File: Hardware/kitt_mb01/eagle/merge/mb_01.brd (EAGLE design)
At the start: 160 x 100 mm, 126 parts, among them CON1 ARDUINO_UNO, IC1.01 RT8293A, IC2.00 BQ24266RGET, IC3.01 LSM9DS1, J1 CON_HEADER_1X06-SMD-RIGHT-ANG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, J2 CON_HEADER_1X06-SMD-RIGHT-ANG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, P2 S2B-PH-K-S(LF)(SN), U1 MCP23017-E, U6.01 TPS61032RSARPSDO-G16, U7.01 SI1922EDH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

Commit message: snapshot of board merge : fancy pants edition -> added posh silk-screen logo    (possibly too large, still)
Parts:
- removed J1, J2: CON_HEADER_1X06-SMD-RIGHT-ANGLED, dp_devices:M1X6_MALE_RIGHT_ANGLED_SMD
- removed JP3: (no value), pinhead:1X18/90
- removed U1: MCP23017-E, kitt.ic:SOIC28-1.27-17.9X7.5MM
- added REF2: REF.LOGO.UASUA, kitt.refs:REF_LOGO_UASUA
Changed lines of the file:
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@@
 <grid distance="12.5" unitdist="mil" unit="mil" style="lines" multiple="1" display="yes" altdistance="0.0125" altunitdist="inch" altunit="inch"/>
 <layers>
-<layer number="1" name="Top" color="4" fill="1" visible="yes" active="yes"/>
-<layer number="2" name="Route2" color="29" fill="0" visible="yes" active="yes"/>
-<layer number="3" name="Route3" color="24" fill="9" visible="yes" active="yes"/>
+<layer number="1" name="Top" color="4" fill="1" visible="no" active="yes"/>
+<layer number="2" name="Route2" color="29" fill="0" visible="no" active="yes"/>
+<layer number="3" name="Route3" color="24" fill="9" visible="no" active="yes"/>
 <layer number="14" name="Route14" color="1" fill="6" visible="no" active="no"/>
 <layer number="15" name="Route15" color="4" fill="6" visible="no" active="no"/>
@@
 <element name="R0.04" library="rcl" package="R1206" value="[0R]" x="53.6575" y="45.085" rot="MR0"/>
 <element name="JMP2" library="jump-0r-smd" package="A0R-JMP" value="0R-JUMPA" x="50.165" y="50.8" rot="R270"/>
-<element name="U1" library="kitt.ic" package="SOIC28-1.27-17.9X7.5MM" value="MCP23017-E" x="22.38375" y="69.37375">
-<attribute name="MF" value="Microchip" x="22.38375" y="69.37375" size="1.016" layer="27" font="vector" display="off"/>
-<attribute name="AVAILABILITY" value="Good" x="22.38375" y="69.37375" size="1.016" layer="27" font="vector" display="off"/>
-<attribute name="MP" value="MCP23017-E/SO" x="22.38375" y="69.37375" size="1.016" layer="27" font="vector" display="off"/>
-<attribute name="PACKAGE" value="SOIC-28 Microchip" x="22.38375" y="69.37375" size="1.016" layer="27" font="vector" display="off"/>
-<attribute name="DESCRIPTION" value="MCP23017 Series 5.5 V 1.7 MHz SMT 16-Bit I2C I/O Expander - SOIC-28" x="22.38375" y="69.37375" size="1.016" layer="27" font="vector" display="off"/>
-<attribute name="PRICE" value="1.15 USD" x="22.38375" y="69.37375" size="1.016" layer="27" font="vector" display="off"/>
-</element>
 <element name="JP2" library="pinhead" package="2X03/90" value="" x="48.5775" y="39.37" rot="R90"/>
-<element name="JP3" library="pinhead" package="1X18/90" value="" x="4.1275" y="52.07" rot="R90"/>
-<element name="J1" library="dp_devices" package="M1X6_MALE_RIGHT_ANGLED_SMD" value="CON_HEADER_1X06-SMD-RIGHT-ANGLED" x="32.0675" y="52.3875" rot="MR270"/>
-<element name="J2" library="dp_devices" package="M1X6_MALE_RIGHT_ANGLED_SMD" value="CON_HEADER_1X06-SMD-RIGHT-ANGLED" x="25.0825" y="30.48" rot="MR0"/>
 <element name="U$5" library="marks" package="PASS-ROUND" value="" x="67.31" y="46.6725"/>
 <element name="R7,05" library="rcl" package="R0603" value="330R" x="97.155" y="27.94" rot="MR0"/>
@@
 <element name="U$9" library="marks" package="PASSER-CIRCLE" value="" x="102.87" y="71.755"/>
 <element name="REF1" library="kitt.refs" package="REF_LAYERS" value="REF.LAYERS" x="102.5525" y="67.945" rot="R270"/>
+<element name="REF2" library="kitt.refs" package="REF_LOGO_UASUA" value="REF.LOGO.UASUA" x="77.63" y="65.405" rot="MR270"/>
 </elements>
 <signals>

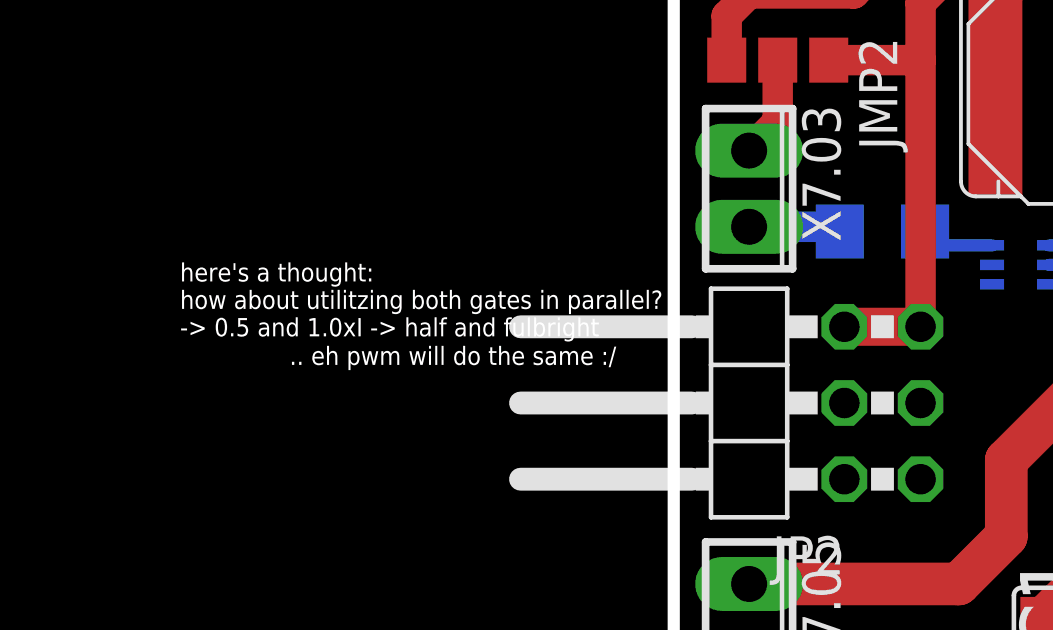
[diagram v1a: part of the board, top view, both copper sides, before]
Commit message: added proper credits in schematics
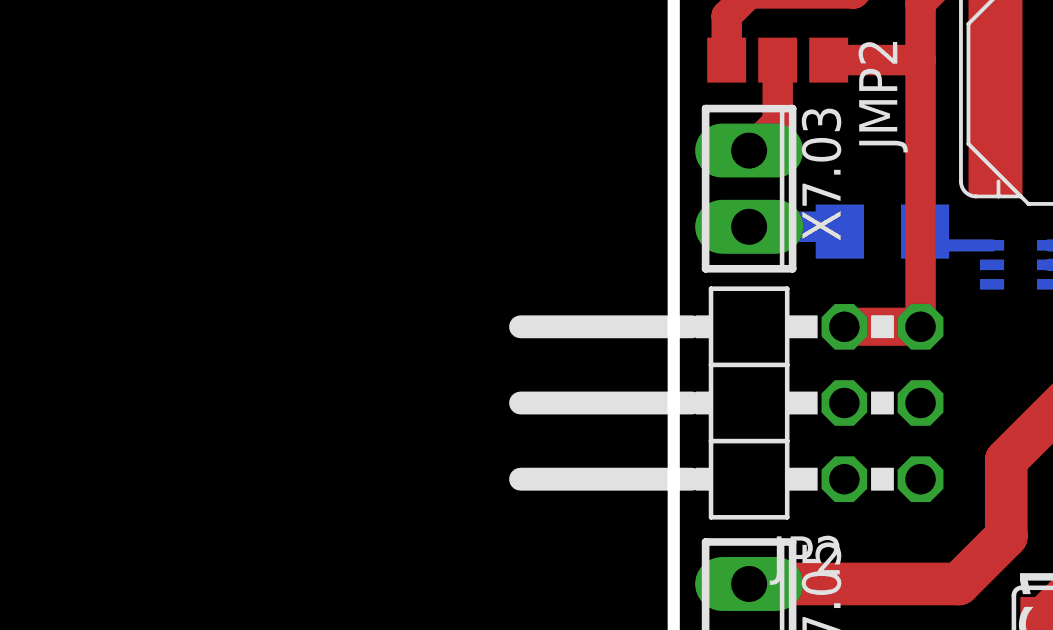
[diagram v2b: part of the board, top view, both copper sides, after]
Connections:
- new net ARDUINO.SCL: IC3.01.2
- new net ARDUINO.SDA: IC3.01.4
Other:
- board text added: "<-- IDK"
- board text added: "ARDUINO<->RAILS"
- board text added: "GROUND POURS"
- board text added: "RAILS POURS"
- board text added: "SPEEDBOARD --> LAPDETECTOR -->"
- board text added: "TODO: COMMAND/BOTTOM LIGHT!!!"
- board text removed: ".. eh pwm will do the same :/"
- board text removed: "here's a thought: how about utilitzing both gates in parallel? -> 0.5 and 1.0xI -> half and fulbright"
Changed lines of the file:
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@@
 <grid distance="12.5" unitdist="mil" unit="mil" style="lines" multiple="1" display="yes" altdistance="0.0125" altunitdist="inch" altunit="inch"/>
 <layers>
-<layer number="1" name="Top" color="4" fill="1" visible="no" active="yes"/>
+<layer number="1" name="Top" color="4" fill="1" visible="yes" active="yes"/>
 <layer number="2" name="Route2" color="29" fill="0" visible="no" active="yes"/>
-<layer number="3" name="Route3" color="24" fill="9" visible="no" active="yes"/>
+<layer number="3" name="Route3" color="24" fill="9" visible="yes" active="yes"/>
 <layer number="14" name="Route14" color="1" fill="6" visible="no" active="no"/>
 <layer number="15" name="Route15" color="4" fill="6" visible="no" active="no"/>
@@
 <text x="45.085" y="47.228125" size="1.778" layer="51" rot="R180">Tail Light --&gt;</text>
 <text x="106.600625" y="46.51375" size="1.778" layer="51">&lt;-- Head Light</text>
-<text x="30.241875" y="41.5925" size="0.6096" layer="46">here's a thought:
-how about utilitzing both gates in parallel?
--&gt; 0.5 and 1.0xI -&gt; half and fulbright</text>
-<text x="33.893125" y="40.64" size="0.6096" layer="46">.. eh pwm will do the same :/</text>
 <hole x="101.6" y="27.94" drill="1.6"/>
+<text x="15.5575" y="52.07" size="1.6764" layer="49" rot="R90">&lt;-- IDK</text>
+<text x="20.32" y="37.7825" size="1.6764" layer="49">SPEEDBOARD --&gt;
+LAPDETECTOR --&gt;</text>
+<text x="70.485" y="11.43" size="1.6764" layer="49">TODO:
+COMMAND/BOTTOM LIGHT!!!</text>
+<text x="70.485" y="8.5725" size="1.778" layer="48">GROUND POURS</text>
+<text x="91.7575" y="8.5725" size="1.778" layer="48">RAILS POURS</text>
+<text x="70.1675" y="6.0325" size="1.778" layer="48">ARDUINO&lt;-&gt;RAILS</text>
 </plain>
 <attributes>
@@
 <wire x1="102.235" y1="59.69" x2="104.775" y2="59.69" width="0" layer="2"/>
 </signal>
+<signal name="ARDUINO.SCL">
+<contactref element="IC3.01" pad="2"/>
+</signal>
+<signal name="ARDUINO.SDA">
+<contactref element="IC3.01" pad="4"/>
+</signal>
 </signals>

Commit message: snapshot of board merge
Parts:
- removed D7.01, D7.02: (no value), led:CHIPLED_1206
- removed R7,03, R7.04: 330R, rcl:R0603
- U$3: value SI1922EDH -> (none); device kitt.ic:SC70-6 -> frames:A4L-LOC
- moved U$3 110.4 mm to (-48.3, -42.5), turned to 0 degrees
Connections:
- removed net N$3: D7.01.C, U$3.6
- removed net N$4: D7.01.A, R7,03.1
- removed net N$5: D7.02.A, R7.04.1
- removed net N$7: D7.02.C, U$3.3
- net +3V3: no longer R7,03.2, R7.04.2
- net GND: no longer U$3.1, U$3.4
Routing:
- net N$7: track 4.12 -> 0.00 mm
- net N$5: track 3.51 -> 0.00 mm
- net GND: track 245.3 -> 242.5 mm
- net N$4: track 1.92 -> 0.00 mm
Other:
- board text added: "D.Hoeginger/A.Gessler"
- board text added: "KITT-MB01 PCB LAYOUT"
- board text added: "Kit for Intelligent and Trainable Trackcars"
- board text removed: "<-- IDK"
- board text removed: "GND@2"
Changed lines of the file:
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@@
 <layers>
 <layer number="1" name="Top" color="4" fill="1" visible="yes" active="yes"/>
-<layer number="2" name="Route2" color="29" fill="0" visible="no" active="yes"/>
+<layer number="2" name="Route2" color="29" fill="0" visible="yes" active="yes"/>
 <layer number="3" name="Route3" color="24" fill="9" visible="yes" active="yes"/>
 <layer number="14" name="Route14" color="1" fill="6" visible="no" active="no"/>
@@
 <wire x1="102.6" y1="73.9" x2="49.1" y2="73.9" width="0.4064" layer="20"/>
 <wire x1="46.7" y1="71.4" x2="46.7" y2="23.1" width="0.4064" layer="20"/>
-<text x="20.16125" y="7.77875" size="1.778" layer="2">GND@2</text>
-<text x="147.32" y="4.60375" size="1.778" layer="2">GND@2</text>
-<text x="143.03375" y="87.78875" size="1.778" layer="2">GND@2</text>
-<text x="8.5725" y="89.8525" size="1.778" layer="2">GND@2</text>
 <text x="48.26" y="64.92875" size="1.9304" layer="25" font="vector">+</text>
 <text x="102.5525" y="35.40125" size="1.016" layer="25" font="vector" rot="R90">SHUNT</text>
@@
 <text x="106.600625" y="46.51375" size="1.778" layer="51">&lt;-- Head Light</text>
 <hole x="101.6" y="27.94" drill="1.6"/>
-<text x="15.5575" y="52.07" size="1.6764" layer="49" rot="R90">&lt;-- IDK</text>
 <text x="20.32" y="37.7825" size="1.6764" layer="49">SPEEDBOARD --&gt;
 LAPDETECTOR --&gt;</text>
@@
 <text x="91.7575" y="8.5725" size="1.778" layer="48">RAILS POURS</text>
 <text x="70.1675" y="6.0325" size="1.778" layer="48">ARDUINO&lt;-&gt;RAILS</text>
+<text x="168.91" y="-22.225" size="1.9304" layer="48" font="vector">D.Hoeginger/A.Gessler</text>
+<text x="114.3" y="-21.9075" size="1.9304" layer="48" font="vector">KITT-MB01 PCB LAYOUT</text>
+<text x="114.3" y="-36.5125" size="1.9304" layer="48" font="vector">Kit for Intelligent and
+Trainable Trackcars</text>
 </plain>
 <attributes>
@@
 <attribute name="MPN" value="" x="102.71125" y="46.51375" size="1.016" layer="27" font="vector" rot="R270" display="off"/>
 </element>
-<element name="D7.01" library="led" package="CHIPLED_1206" value="" x="14.049375" y="43.100625" rot="R270"/>
-<element name="U$3" library="kitt.ic" package="SC70-6" value="SI1922EDH" x="18.176875" y="45.640625" rot="R90"/>
-<element name="R7,03" library="rcl" package="R0603" value="330R" x="14.049375" y="44.688125"/>
-<element name="R7.04" library="rcl" package="R0603" value="330R" x="14.049375" y="46.593125"/>
-<element name="D7.02" library="led" package="CHIPLED_1206" value="" x="14.049375" y="48.180625" rot="R270"/>
 <element name="R0.02" library="rcl" package="R1206" value="SHUNT" x="51.7525" y="56.753125" rot="R270"/>
 <element name="D7.03" library="led" package="CHIPLED_1206" value="" x="101.6" y="54.61" rot="MR90"/>
@@
 <element name="REF1" library="kitt.refs" package="REF_LAYERS" value="REF.LAYERS" x="102.5525" y="67.945" rot="R270"/>
 <element name="REF2" library="kitt.refs" package="REF_LOGO_UASUA" value="REF.LOGO.UASUA" x="77.63" y="65.405" rot="MR270"/>
+<element name="U$3" library="frames" package="A4L-LOC" value="" x="-48.26" y="-42.545"/>
 </elements>
 <signals>
@@
 <wire x1="92.948125" y1="40.9575" x2="94.853125" y2="39.0525" width="1.6764" layer="1"/>
 <wire x1="94.853125" y1="39.0525" x2="100.0125" y2="39.0525" width="1.6764" layer="1"/>
-<contactref element="U$3" pad="1"/>
-<contactref element="U$3" pad="4"/>
-<wire x1="17.226875" y1="46.290625" x2="17.844375" y2="46.290625" width="0.4064" layer="1"/>
-<wire x1="17.844375" y1="46.290625" x2="18.176875" y2="45.958125" width="0.4064" layer="1"/>
-<wire x1="18.176875" y1="45.958125" x2="18.176875" y2="45.323125" width="0.4064" layer="1"/>
-<wire x1="18.176875" y1="45.323125" x2="18.509375" y2="44.990625" width="0.4064" layer="1"/>
-<wire x1="19.126875" y1="44.990625" x2="18.509375" y2="44.990625" width="0.4064" layer="1"/>
 <wire x1="69.8025" y1="41.91" x2="67.945" y2="41.91" width="0.4064" layer="1"/>
 <wire x1="67.945" y1="41.91" x2="66.28" y2="41.91" width="0.4064" layer="1"/>
@@
 <wire x1="103.505" y1="27.785" x2="103.35" y2="27.94" width="0.6096" layer="16"/>
 <wire x1="89.349375" y1="47.550625" x2="88.9" y2="47.3225" width="0" layer="19" extent="1-16"/>
-<wire x1="19.126875" y1="44.990625" x2="48.26" y2="55.331125" width="0" layer="19" extent="1-1"/>
 </signal>
 <signal name="+12V">
@@
 <wire x1="84.29625" y1="43.4975" x2="84.29625" y2="43.244375" width="0.254" layer="1"/>
 <wire x1="84.29625" y1="43.244375" x2="84.61375" y2="43.00625" width="0.254" layer="1"/>
-<contactref element="R7.04" pad="2"/>
-<contactref element="R7,03" pad="2"/>
 <contactref element="R7.01" pad="2"/>
 <contactref element="R7,01" pad="2"/>
@@
 <wire x1="51.865" y1="50.8" x2="54.9275" y2="50.8" width="1.016" layer="1"/>
 <wire x1="76.835" y1="42.148125" x2="77.94625" y2="42.148125" width="0" layer="19" extent="1-3"/>
-<wire x1="14.899375" y1="46.593125" x2="51.865" y2="50.8" width="0" layer="19" extent="1-1"/>
-<wire x1="14.899375" y1="44.688125" x2="14.899375" y2="46.593125" width="0" layer="19" extent="1-1"/>
 </signal>
 <signal name="N$17">
@@
 <wire x1="60.6275" y1="62.70625" x2="58.57875" y2="62.70875" width="0" layer="19" extent="1-1"/>
 </signal>
-<signal name="N$3">
-<contactref element="D7.01" pad="C"/>
-<contactref element="U$3" pad="6"/>
-<wire x1="15.539375" y1="43.100625" x2="15.799375" y2="43.100625" width="0.4064" layer="1"/>
-<wire x1="15.799375" y1="43.100625" x2="17.226875" y2="44.990625" width="0" layer="19" extent="1-1"/>
-</signal>
-<signal name="N$4">
-<contactref element="R7,03" pad="1"/>
-<contactref element="D7.01" pad="A"/>
-<wire x1="13.316875" y1="43.105625" x2="12.299375" y2="43.100625" width="0.4064" layer="1"/>
-<wire x1="13.199375" y1="43.100625" x2="12.299375" y2="43.100625" width="0.4064" layer="1"/>
-<wire x1="13.316875" y1="43.105625" x2="13.199375" y2="44.688125" width="0" layer="19" extent="1-1"/>
-</signal>
-<signal name="N$5">
-<contactref element="R7.04" pad="1"/>
-<contactref element="D7.02" pad="A"/>
-<wire x1="13.316875" y1="48.175625" x2="12.299375" y2="48.180625" width="0.4064" layer="1"/>
-<wire x1="13.199375" y1="46.593125" x2="13.199375" y2="48.180625" width="0.4064" layer="1"/>
-<wire x1="13.199375" y1="48.180625" x2="12.299375" y2="48.180625" width="0.4064" layer="1"/>
-</signal>
-<signal name="N$7">
-<contactref element="D7.02" pad="C"/>
-<contactref element="U$3" pad="3"/>
-<wire x1="18.796875" y1="46.290625" x2="17.859375" y2="47.228125" width="0.4064" layer="1"/>
-<wire x1="17.859375" y1="47.228125" x2="16.051875" y2="47.228125" width="0.4064" layer="1"/>
-<wire x1="16.051875" y1="47.228125" x2="15.799375" y2="48.180625" width="0.4064" layer="1"/>
-<wire x1="18.796875" y1="46.290625" x2="19.126875" y2="46.290625" width="0" layer="19" extent="1-1"/>
-</signal>
 <signal name="N$25">
